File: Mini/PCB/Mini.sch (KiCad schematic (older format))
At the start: 5 parts, among them J1 Conn_01x09_Female, K1 KeyLedDiode, K2 KeyLedDiode, K3 KeyLedDiode, K4 KeyLedDiode

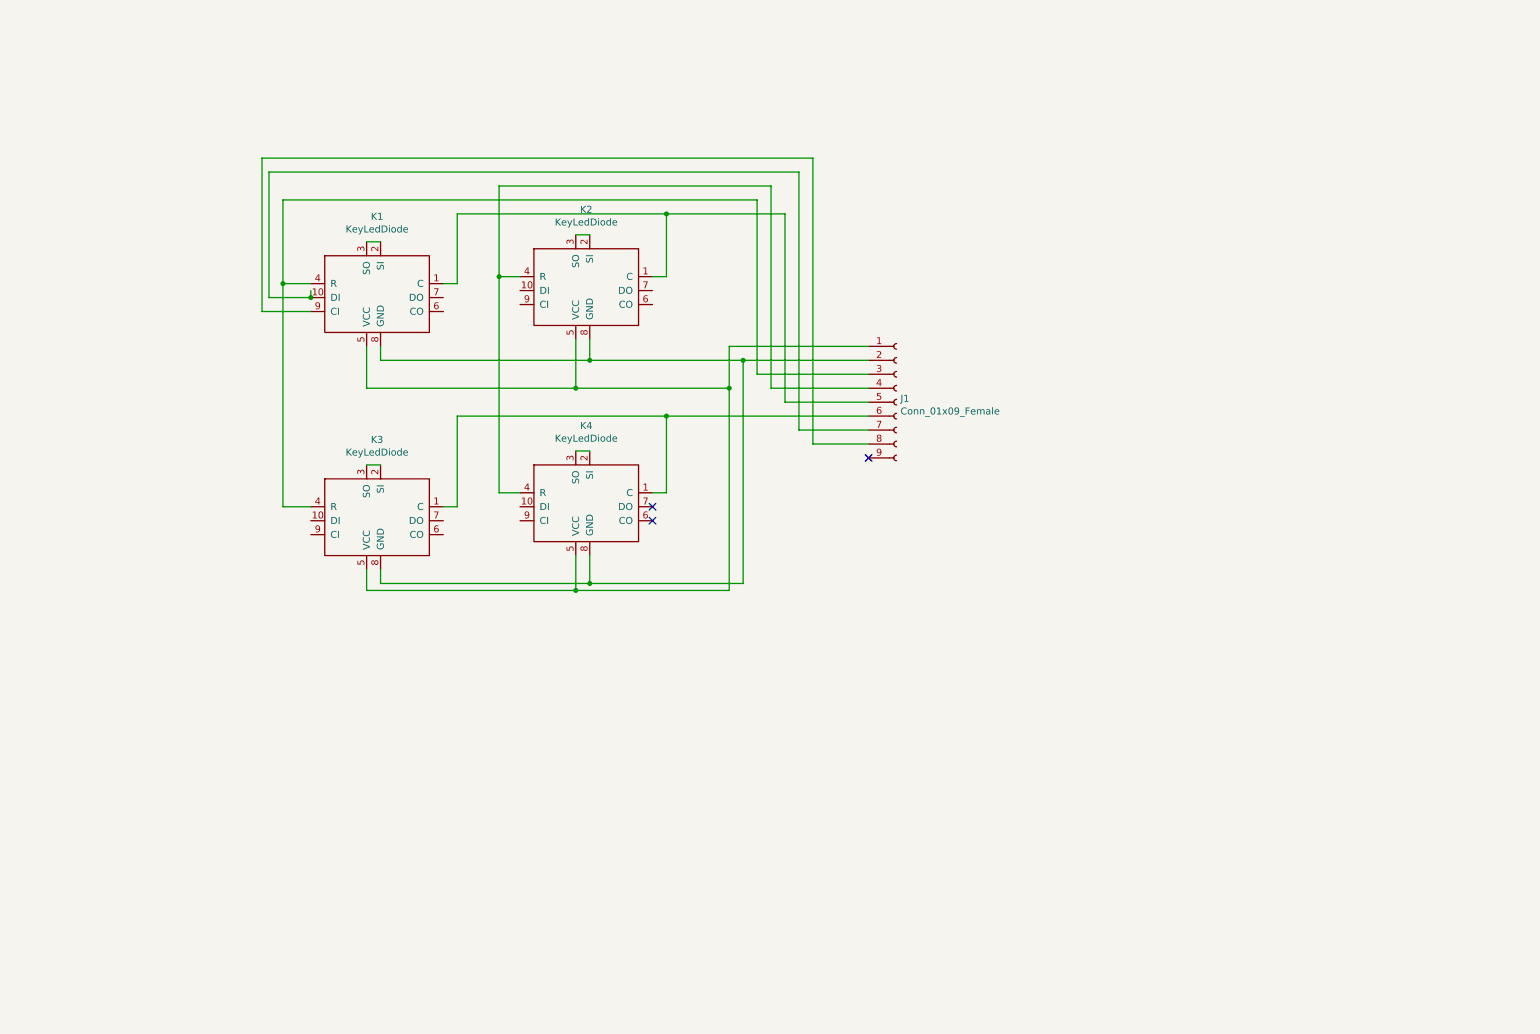
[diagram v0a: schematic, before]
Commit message: Adding schematics for demux, register, and dinn9.  Adding all components to schematic.
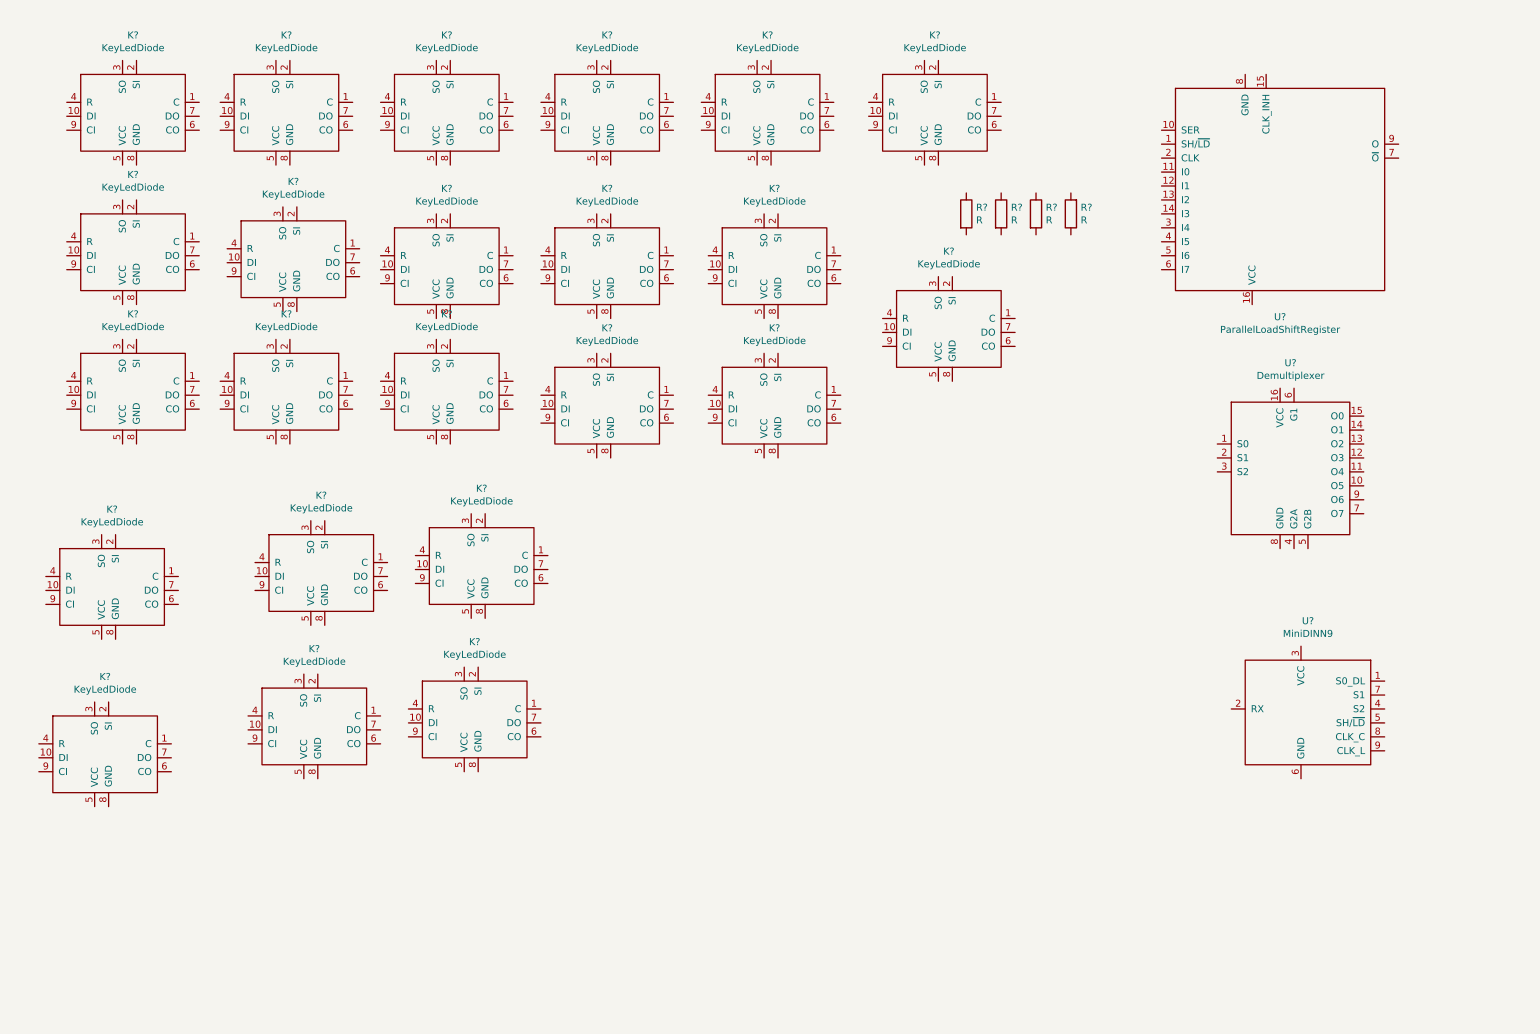
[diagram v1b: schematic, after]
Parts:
- removed J1: Conn_01x09_Female, Mini:MiniDin9, symbol Connector:Conn_01x09_Female
- removed K1, K2, K3, K4: KeyLedDiode, Mini:KeyLedDiode, symbol Mini:KeyLedDiode
- added K? (x23): KeyLedDiode, symbol Mini:KeyLedDiode
- added R? (x4): R, symbol Device:R
- added U?: MiniDINN9, symbol Mini:MiniDINN9
- added U?: Demultiplexer, symbol Mini:Demultiplexer
- added U?: ParallelLoadShiftRegister, symbol Mini:ParallelLoadShiftRegister
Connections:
- no-connect marks 3 -> 0

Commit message: Adding R2L/L2R and 2key variants of key footprints.
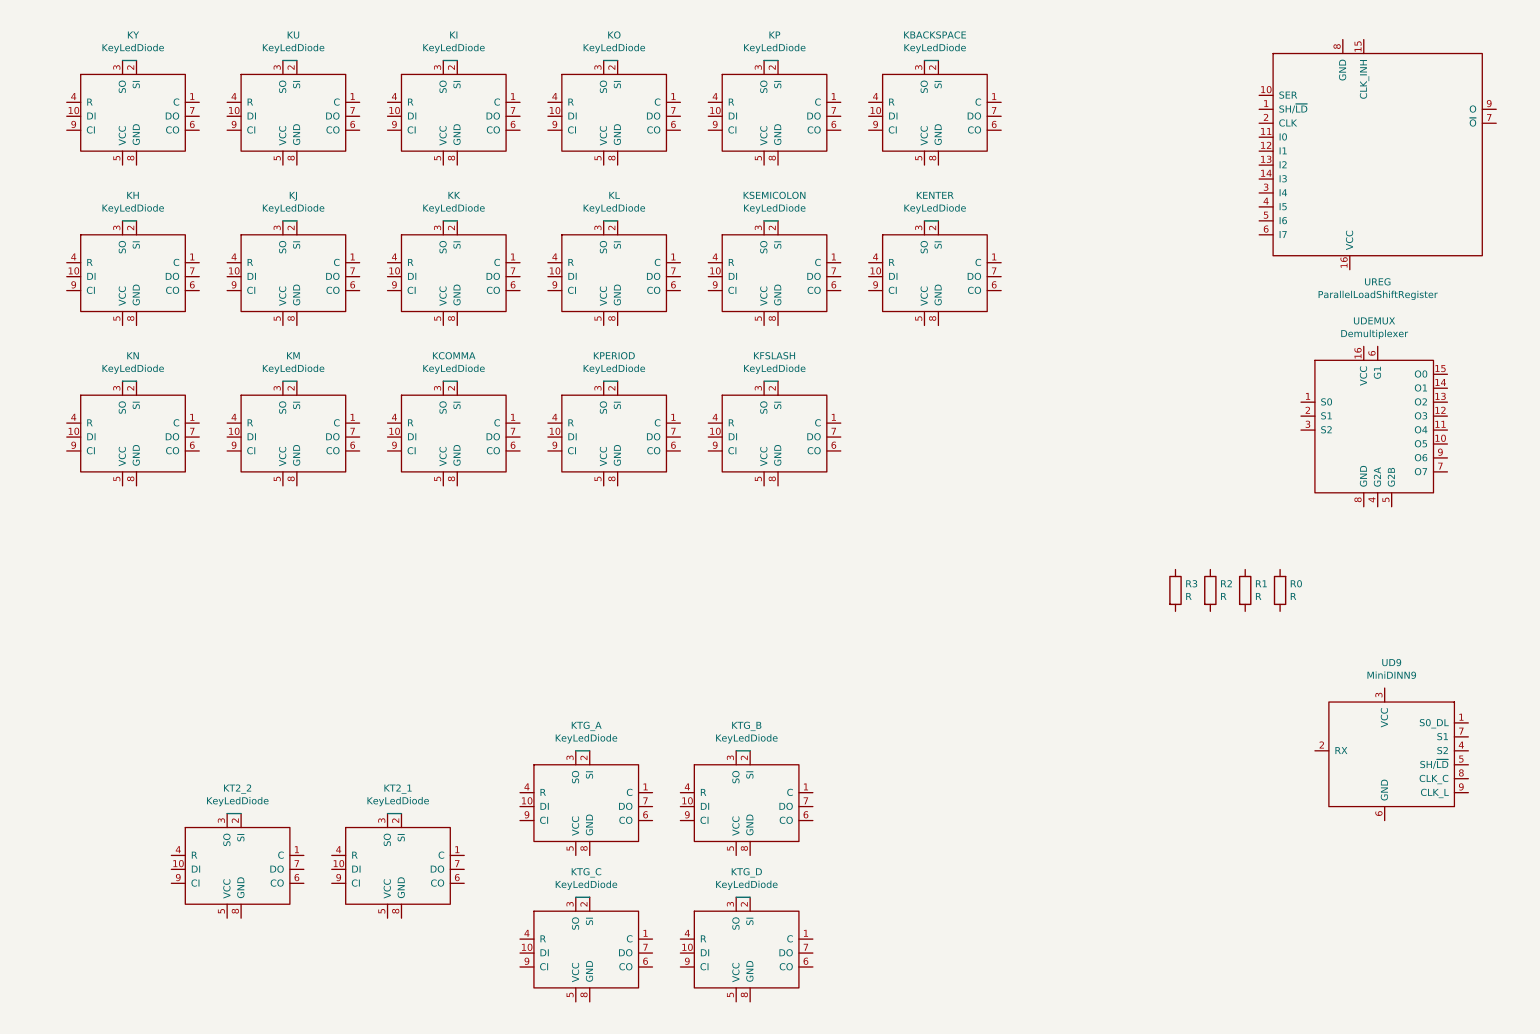
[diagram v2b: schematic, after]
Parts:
- gave numbers to parts that had none: 30
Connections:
- net at KY.2 (SI): now also KY.3 (SO)
- net at KU.2 (SI): now also KU.3 (SO)
- net at KI.2 (SI): now also KI.3 (SO)
- net at KO.2 (SI): now also KO.3 (SO)
- net at KP.2 (SI): now also KP.3 (SO)
- net at KBACKSPACE.2 (SI): now also KBACKSPACE.3 (SO)
- net at KENTER.2 (SI): now also KENTER.3 (SO)
- net at KH.2 (SI): now also KH.3 (SO)
- net at KN.2 (SI): now also KN.3 (SO)
- net at KJ.2 (SI): now also KJ.3 (SO)
- net at KM.2 (SI): now also KM.3 (SO)
- net at KK.2 (SI): now also KK.3 (SO)
- net at KCOMMA.2 (SI): now also KCOMMA.3 (SO)
- net at KL.2 (SI): now also KL.3 (SO)
- net at KPERIOD.2 (SI): now also KPERIOD.3 (SO)
- net at KSEMICOLON.2 (SI): now also KSEMICOLON.3 (SO)
- net at KFSLASH.2 (SI): now also KFSLASH.3 (SO)
- net at KT2_1.2 (SI): now also KT2_1.3 (SO)
- net at KT2_2.2 (SI): now also KT2_2.3 (SO)
- net at KTG_A.2 (SI): now also KTG_A.3 (SO)
- net at KTG_B.2 (SI): now also KTG_B.3 (SO)
- net at KTG_C.2 (SI): now also KTG_C.3 (SO)
- net at KTG_D.2 (SI): now also KTG_D.3 (SO)
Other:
- moved on the sheet: KCOMMA, KENTER, KFSLASH, KH, KI, KJ, KK, KL, KM, KN, KO, KP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

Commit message: Assigning footprints to R.H. schematic.
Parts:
- KBACKSPACE1: renamed from KBACKSPACE; footprint (none) -> Mini:KeyLedDiodeR2L
- KCOMMA1: renamed from KCOMMA; footprint (none) -> Mini:KeyLedDiodeR2L
- KENTER1: renamed from KENTER; footprint (none) -> Mini:KeyLedDiodeL2R
- KFSLASH1: renamed from KFSLASH; footprint (none) -> Mini:KeyLedDiodeR2L
- KH1: renamed from KH; footprint (none) -> Mini:KeyLedDiodeL2R
- KI1: renamed from KI; footprint (none) -> Mini:KeyLedDiodeR2L
- KJ1: renamed from KJ; footprint (none) -> Mini:KeyLedDiodeL2R
- KK1: renamed from KK; footprint (none) -> Mini:KeyLedDiodeL2R
- KL1: renamed from KL; footprint (none) -> Mini:KeyLedDiodeL2R
- KM1: renamed from KM; footprint (none) -> Mini:KeyLedDiodeR2L
- KN1: renamed from KN; footprint (none) -> Mini:KeyLedDiodeR2L
- KO1: renamed from KO; footprint (none) -> Mini:KeyLedDiodeR2L
- KP1: renamed from KP; footprint (none) -> Mini:KeyLedDiodeR2L
- KPERIOD1: renamed from KPERIOD; footprint (none) -> Mini:KeyLedDiodeR2L
- KSEMICOLON1: renamed from KSEMICOLON; footprint (none) -> Mini:KeyLedDiodeL2R
- KT2_1: footprint (none) -> Mini:Key2LedDiodeL2R
- KT2_2: footprint (none) -> Mini:Key2LedDiodeR2L
- KTG_A1: renamed from KTG_A; footprint (none) -> Mini:KeyLedDiodeL2R
- KTG_B1: renamed from KTG_B; footprint (none) -> Mini:KeyLedDiodeL2R
- KTG_C1: renamed from KTG_C; footprint (none) -> Mini:KeyLedDiodeR2L
- KTG_D1: renamed from KTG_D; footprint (none) -> Mini:KeyLedDiodeR2L
- KU1: renamed from KU; footprint (none) -> Mini:KeyLedDiodeR2L
- KY1: renamed from KY; footprint (none) -> Mini:KeyLedDiodeR2L
- R0, R1, R2, R3: footprint (none) -> Mini:PullupResistor
- UD9: footprint (none) -> Mini:MiniDin9
- UDEMUX1: renamed from UDEMUX; footprint (none) -> Mini:DualInlineMicrochip2x8
- UREG1: renamed from UREG; footprint (none) -> Mini:DualInlineMicrochip2x8

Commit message: Wiring up all pins on schematic.
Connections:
- net S0_DL: now reaches UD9.1 (S0_DL)
- net S0_DL: now also KBACKSPACE1.10 (DI), UDEMUX1.1 (S0)
- net RX: now reaches UD9.2 (RX)
- net RX: now also UREG1.9 (O)
- net VCC: now reaches UD9.3 (VCC)
- net VCC: now also KBACKSPACE1.5 (VCC), KCOMMA1.5 (VCC), KENTER1.5 (VCC), KFSLASH1.5 (VCC), KH1.5 (VCC), KI1.5 (VCC), KJ1.5 (VCC), KK1.5 (VCC), KL1.5 (VCC), KM1.5 (VCC), KN1.5 (VCC), KO1.5 (VCC), KP1.5 (VCC), KPERIOD1.5 (VCC), KSEMICOLON1.5 (VCC), KT2_1.5 (VCC), KT2_2.5 (VCC), KTG_A1.5 (VCC), KTG_B1.5 (VCC), KTG_C1.5 (VCC), KTG_D1.5 (VCC), KU1.5 (VCC), KY1.5 (VCC), R0.1, R1.2, R2.2, R3.2, UDEMUX1.16 (VCC), UDEMUX1.6 (G1), UREG1.16 (VCC)
- net S2: now reaches UD9.4 (S2)
- net S2: now also UDEMUX1.3 (S2)
- net SH_LD: now reaches UD9.5 (SH/~LD)
- net SH_LD: now also UREG1.1 (SH/~LD)
- net GND: now reaches UD9.6 (GND)
- net GND: now also KBACKSPACE1.8 (GND), KCOMMA1.8 (GND), KENTER1.8 (GND), KFSLASH1.8 (GND), KH1.8 (GND), KI1.8 (GND), KJ1.8 (GND), KK1.8 (GND), KL1.8 (GND), KM1.8 (GND), KN1.8 (GND), KO1.8 (GND), KP1.8 (GND), KPERIOD1.8 (GND), KSEMICOLON1.8 (GND), KT2_1.8 (GND), KT2_2.8 (GND), KTG_A1.8 (GND), KTG_B1.8 (GND), KTG_C1.8 (GND), KTG_D1.8 (GND), KU1.8 (GND), KY1.8 (GND), UDEMUX1.4 (G2A), UDEMUX1.5 (G2B), UDEMUX1.8 (GND), UREG1.10 (SER), UREG1.11 (I0), UREG1.12 (I1), UREG1.13 (I2), UREG1.14 (I3), UREG1.15 (CLK_INH), UREG1.8 (GND)
- net S1: now reaches UD9.7 (S1)
- net S1: now also UDEMUX1.2 (S1)
- net CLK_C: now reaches UD9.8 (CLK_C)
- net CLK_C: now also UREG1.2 (CLK)
- net CLK_L: now reaches UD9.9 (CLK_L)
- net CLK_L: now also KBACKSPACE1.9 (CI)
- net R5: now reaches UDEMUX1.10 (O5)
- net R5: now also KPERIOD1.4 (R)
- net R4: now reaches UDEMUX1.11 (O4)
- net R4: now also KCOMMA1.4 (R), KI1.4 (R), KK1.4 (R)
- net R3: now reaches UDEMUX1.12 (O3)
- net R3: now also KJ1.4 (R), KM1.4 (R), KTG_B1.4 (R), KU1.4 (R)
- net R2: now reaches UDEMUX1.13 (O2)
- net R2: now also KH1.4 (R), KN1.4 (R), KTG_A1.4 (R), KY1.4 (R)
- net R1: now reaches UDEMUX1.14 (O1)
- net R1: now also KT2_1.4 (R), KTG_C1.4 (R)
- net R0: now reaches UDEMUX1.15 (O0)
- net R0: now also KT2_2.4 (R), KTG_D1.4 (R)
- net R7: now reaches UDEMUX1.7 (O7)
- net R7: now also KBACKSPACE1.4 (R), KENTER1.4 (R)
- net R6: now reaches UDEMUX1.9 (O6)
- net R6: now also KFSLASH1.4 (R), KP1.4 (R), KSEMICOLON1.4 (R)
- net C3: now reaches UREG1.3 (I4)
- net C3: now also KTG_A1.1 (C), KTG_B1.1 (C), KTG_C1.1 (C), KTG_D1.1 (C), R3.1
- net C2: now reaches UREG1.4 (I5)
- net C2: now also KCOMMA1.1 (C), KFSLASH1.1 (C), KM1.1 (C), KN1.1 (C), KPERIOD1.1 (C), KT2_1.1 (C), KT2_2.1 (C), R2.1
- net C1: now reaches UREG1.5 (I6)
- net C1: now also KENTER1.1 (C), KH1.1 (C), KJ1.1 (C), KK1.1 (C), KL1.1 (C), KSEMICOLON1.1 (C), R1.1
- net C0: now reaches UREG1.6 (I7)
- net C0: now also KBACKSPACE1.1 (C), KI1.1 (C), KO1.1 (C), KP1.1 (C), KU1.1 (C), KY1.1 (C), R0.2
- net at KY1.10 (DI): now also KU1.7 (DO)
- net at KY1.6 (CO): now also KH1.9 (CI)
- net at KY1.7 (DO): now also KH1.10 (DI)
- net at KY1.9 (CI): now also KU1.6 (CO)
- net at KU1.10 (DI): now also KI1.7 (DO)
- net at KU1.9 (CI): now also KI1.6 (CO)
- net at KI1.10 (DI): now also KO1.7 (DO)
- net at KI1.9 (CI): now also KO1.6 (CO)
- net at KO1.10 (DI): now also KP1.7 (DO)
- net at KO1.4 (R): now also KL1.4 (R)
- net at KO1.9 (CI): now also KP1.6 (CO)
- net at KP1.10 (DI): now also KBACKSPACE1.7 (DO)
- net at KP1.9 (CI): now also KBACKSPACE1.6 (CO)
- net at KENTER1.10 (DI): now also KSEMICOLON1.7 (DO)
- net at KENTER1.6 (CO): now also KFSLASH1.9 (CI)
- net at KENTER1.7 (DO): now also KFSLASH1.10 (DI)
- net at KENTER1.9 (CI): now also KSEMICOLON1.6 (CO)
- net at KH1.6 (CO): now also KJ1.9 (CI)
- net at KH1.7 (DO): now also KJ1.10 (DI)
- net at KN1.10 (DI): now also KM1.7 (DO)
- net at KN1.6 (CO): now also KTG_A1.9 (CI)
- net at KN1.7 (DO): now also KTG_A1.10 (DI)
- net at KN1.9 (CI): now also KM1.6 (CO)
- net at KJ1.6 (CO): now also KK1.9 (CI)
- net at KJ1.7 (DO): now also KK1.10 (DI)
- net at KM1.10 (DI): now also KCOMMA1.7 (DO)
- net at KM1.9 (CI): now also KCOMMA1.6 (CO)
- net at KK1.6 (CO): now also KL1.9 (CI)
- net at KK1.7 (DO): now also KL1.10 (DI)
- net at KCOMMA1.10 (DI): now also KPERIOD1.7 (DO)
- net at KCOMMA1.9 (CI): now also KPERIOD1.6 (CO)
- net at KL1.6 (CO): now also KSEMICOLON1.9 (CI)
- net at KL1.7 (DO): now also KSEMICOLON1.10 (DI)
- net at KPERIOD1.10 (DI): now also KFSLASH1.7 (DO)
- net at KPERIOD1.9 (CI): now also KFSLASH1.6 (CO)
- net at KT2_1.10 (DI): now also KTG_C1.7 (DO)
- net at KT2_1.6 (CO): now also KT2_2.9 (CI)
- net at KT2_1.7 (DO): now also KT2_2.10 (DI)
- net at KT2_1.9 (CI): now also KTG_C1.6 (CO)
- net at KTG_A1.6 (CO): now also KTG_B1.9 (CI)
- net at KTG_A1.7 (DO): now also KTG_B1.10 (DI)
- net at KTG_B1.6 (CO): now also KTG_D1.9 (CI)
- net at KTG_B1.7 (DO): now also KTG_D1.10 (DI)
- net at KTG_C1.10 (DI): now also KTG_D1.7 (DO)
- net at KTG_C1.9 (CI): now also KTG_D1.6 (CO)
- no-connect marks 0 -> 3
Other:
- moved on the sheet: KT2_1, KT2_2, KTG_A1, KTG_B1, KTG_C1, KTG_D1, R0, R1, R2, R3, UD9

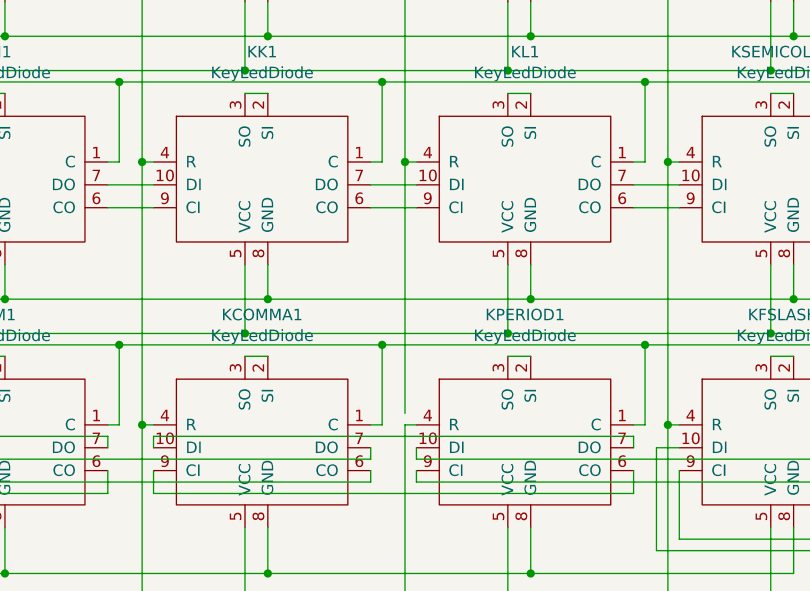
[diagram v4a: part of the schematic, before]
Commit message: Wiring everything except LED VCC/GND.
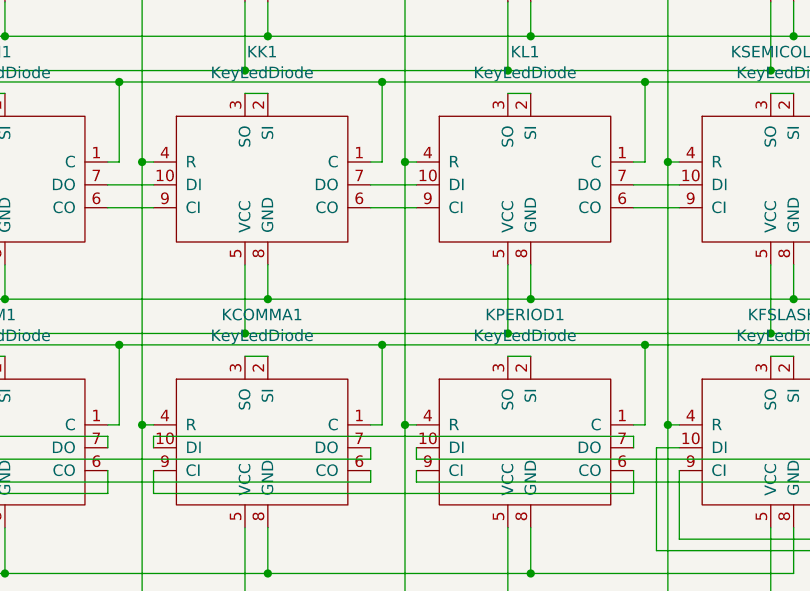
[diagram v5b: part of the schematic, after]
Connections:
- net R5: now also KL1.4 (R), KO1.4 (R)
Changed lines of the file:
@@
 	4200 3400 4250 3400
-Wire Wire Line
-	4200 3350 4200 2250
 Wire Wire Line
 	4200 2250 4250 2250
@@
 Wire Wire Line
 	800  3450 800  3500
+Wire Wire Line
+	4200 2250 4200 3400
+Connection ~ 4200 3400
 $EndSCHEMATC
